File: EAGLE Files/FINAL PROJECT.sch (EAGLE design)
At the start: 11 parts, among them J1 BATTERY, U1 9_to_3.3_VREG

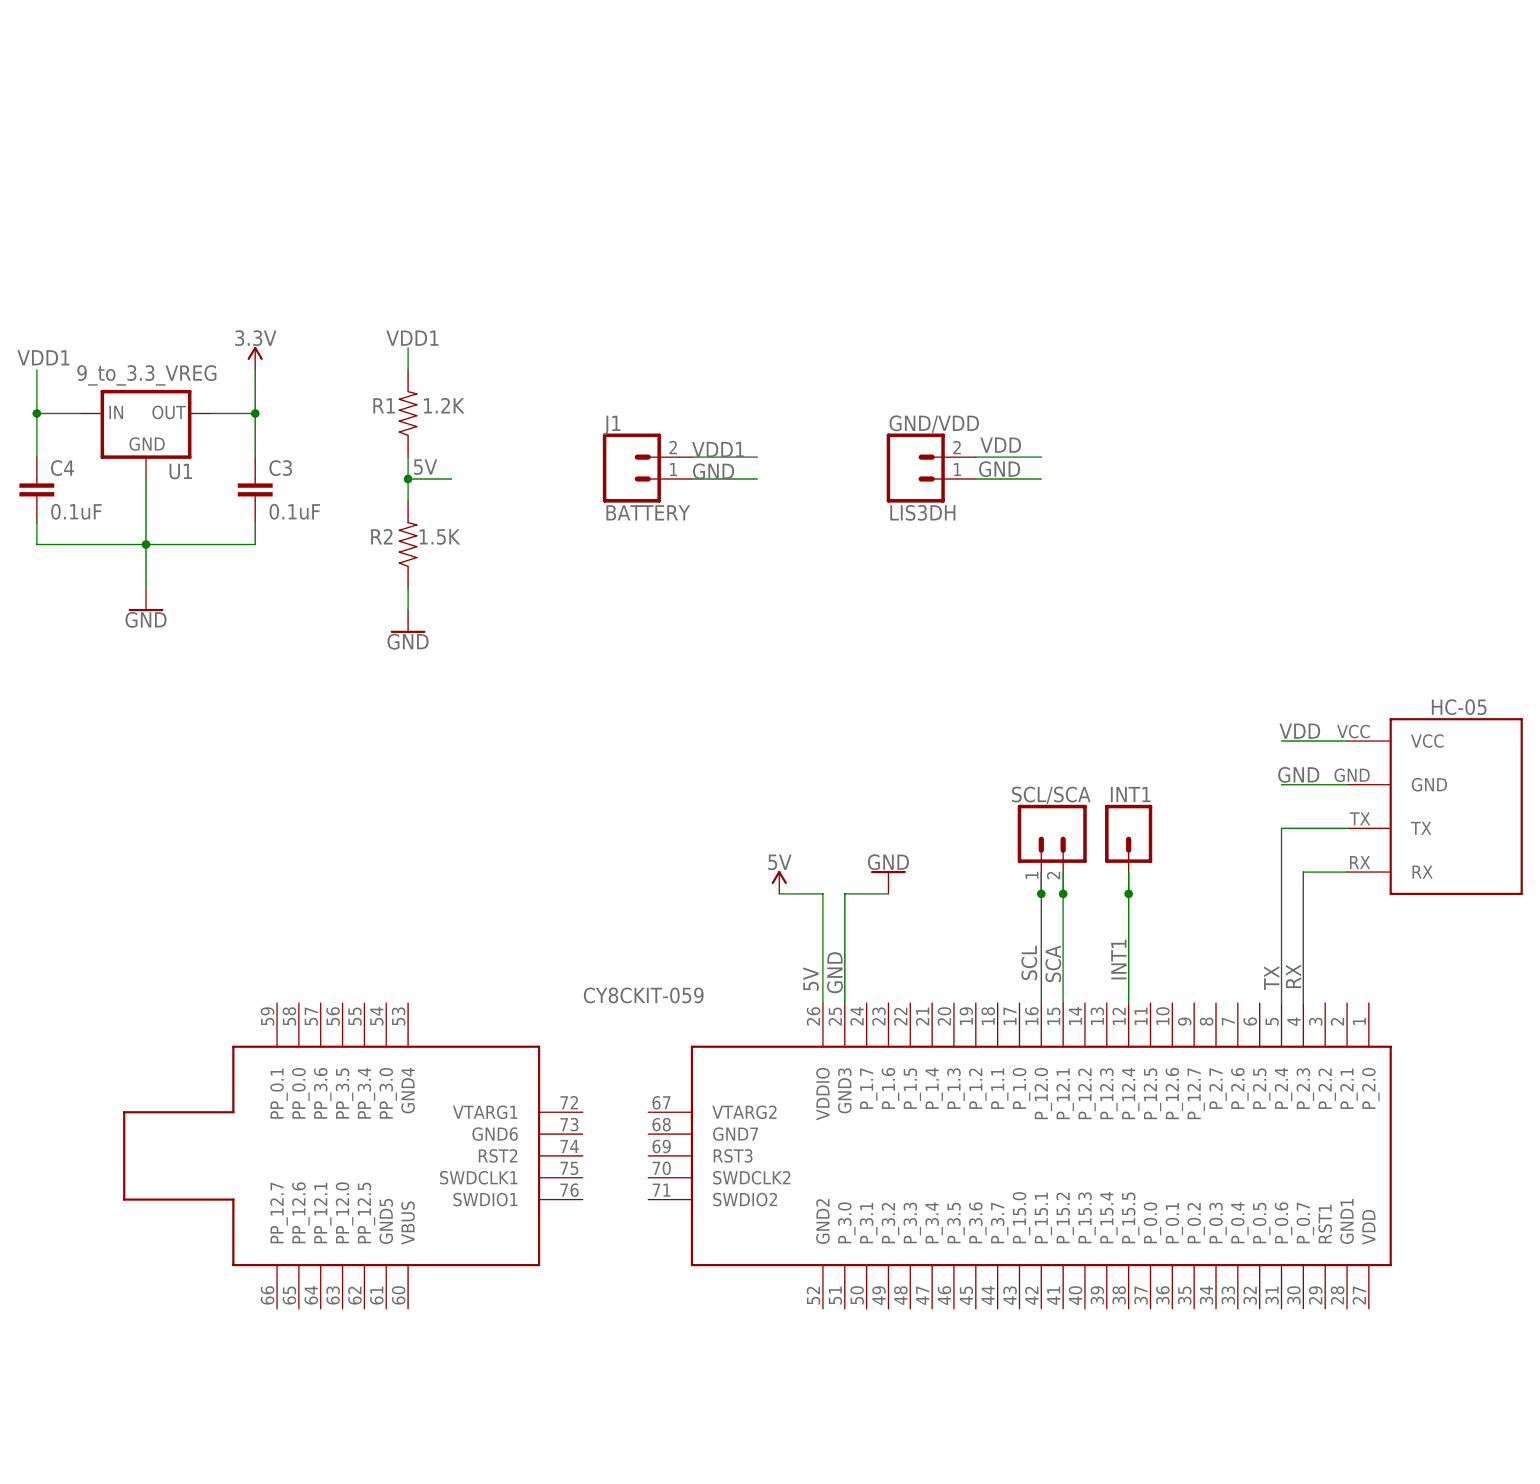
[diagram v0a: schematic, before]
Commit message: EAGLE-Files-added LED
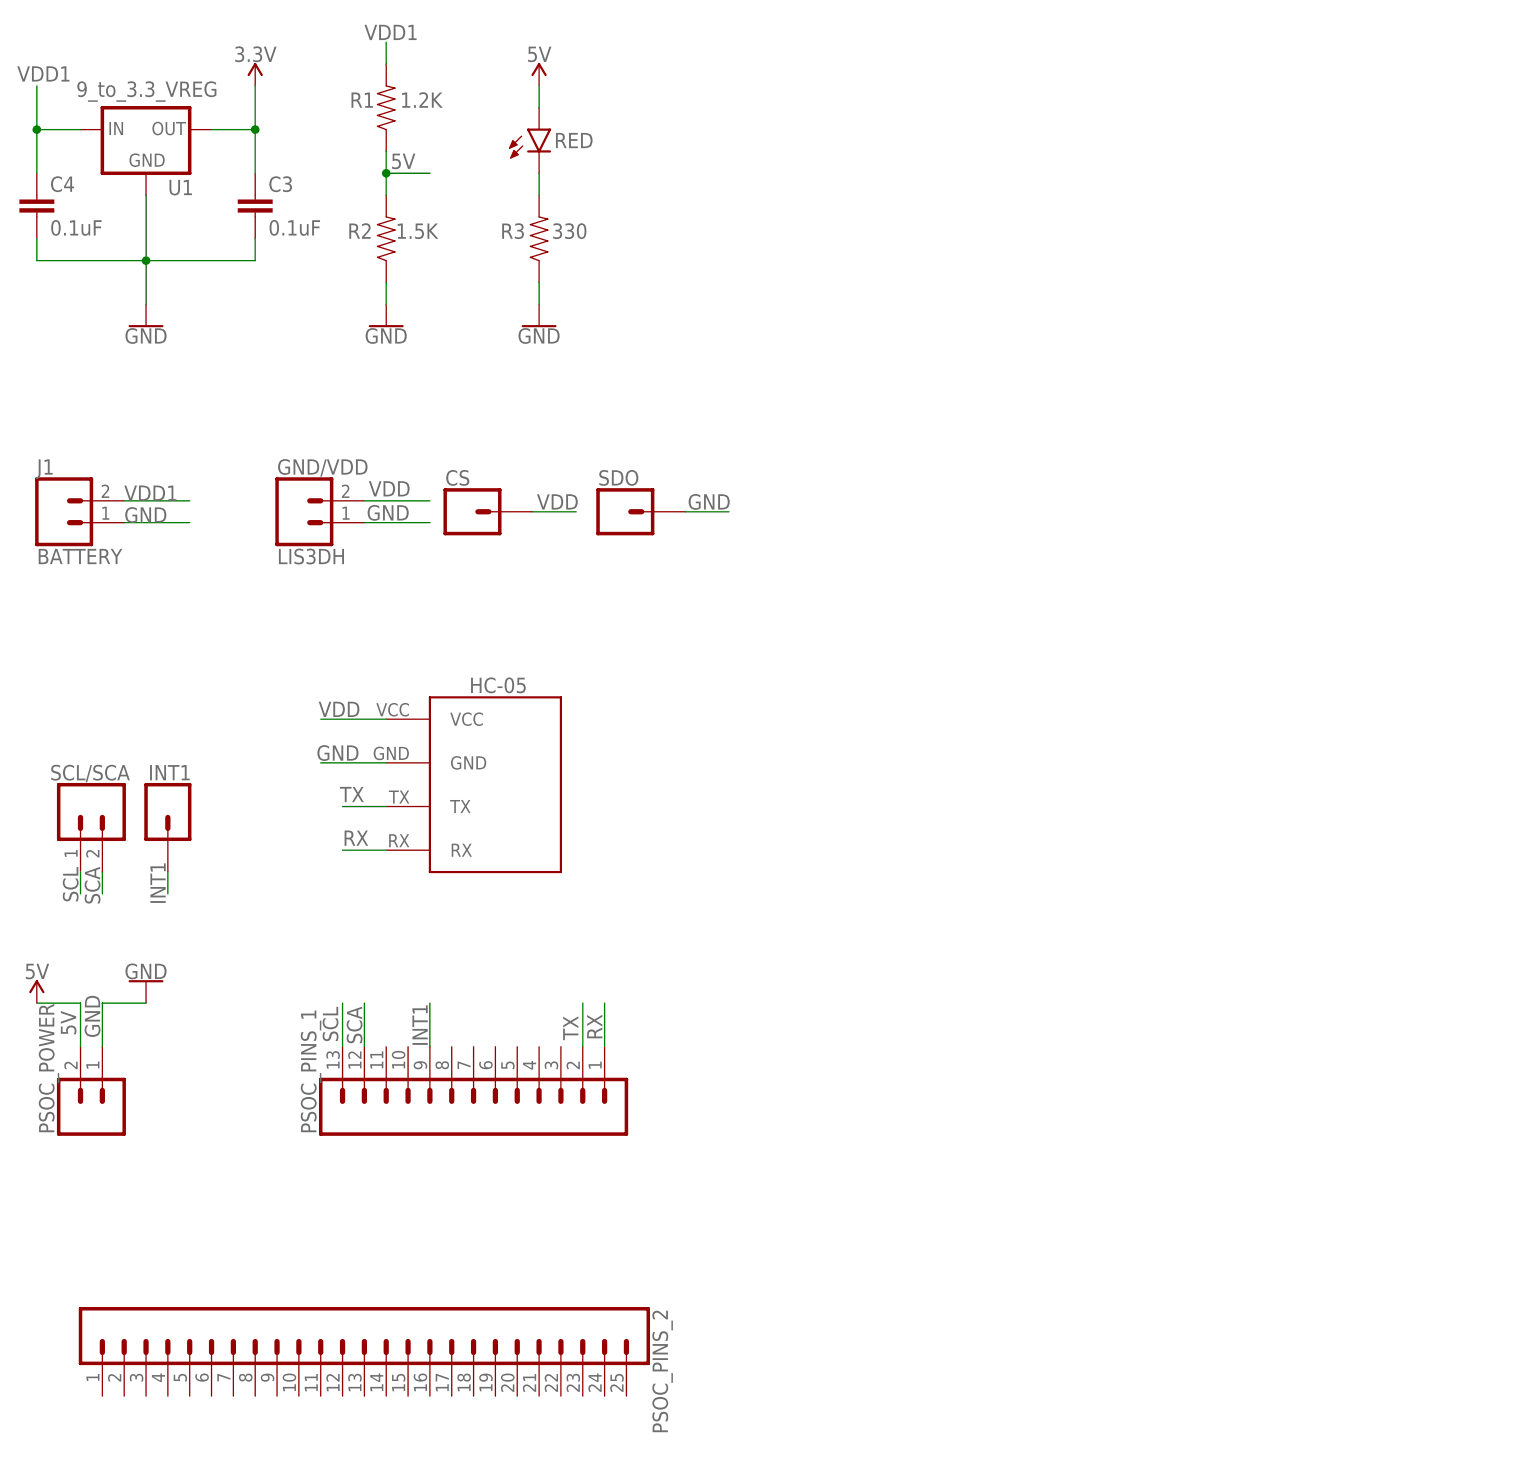
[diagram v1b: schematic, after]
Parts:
- removed U$1: CY8CKIT-059, CYKIT:CY8CKIT-059
- added CS, SDO: (no value), SparkFun-Connectors:CONN_01
- added PSOC_PINS_1: (no value), SparkFun-Connectors:CONN_13
- added PSOC_PINS_2: (no value), SparkFun-Connectors:CONN_25
- added PSOC_POWER: (no value), SparkFun-Connectors:CONN_02
- added R3: 330, SparkFun-Resistors:330OHM-HORIZ-1/10W-5%
- added RED: (no value), SparkFun-LED:LED3MM
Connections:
- new net N$1: R3.2, RED.C
- net 5V: now also PSOC_POWER.2, RED.A; no longer U$1.VDDIO
- net GND: now also PSOC_POWER.1, R3.1, SDO.1; no longer U$1.GND3
- net INT1: now also PSOC_PINS_1.9; no longer U$1.P_12.4
- net RX: now also PSOC_PINS_1.1; no longer U$1.P_2.3
- net SCA: now also PSOC_PINS_1.12; no longer U$1.P_12.1
- net SCL: now also PSOC_PINS_1.13; no longer U$1.P_12.0
- net TX: now also PSOC_PINS_1.2; no longer U$1.P_2.4
- net VDD: now also CS.1
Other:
- moved on the sheet: C3, C4, GND/VDD, HC-05, INT1, J1, R1, R2, SCL/SCA, U1
